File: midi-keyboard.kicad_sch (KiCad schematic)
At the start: 69 parts, among them J1 Conn_01x04, SW1 SW_Push_45deg, SW10 SW_Push_45deg, SW11 SW_Push_45deg, SW12 SW_Push_45deg, SW13 SW_Push_45deg, SW15 SW_Push_45deg, SW16 SW_Push_45deg, SW17 SW_Push_45deg, SW18 SW_Push_45deg, SW19 SW_Push_45deg, SW2 SW_Push_45deg, SW20 SW_Push_45deg, SW22 SW_Push_45deg, SW23 SW_Push_45deg, SW24 SW_Push_45deg, SW25 SW_Push_45deg, SW26 SW_Push_45deg, SW29 SW_Push_45deg, SW3 SW_Push_45deg, SW30 SW_Push_45deg, SW31 SW_Push_45deg, SW32 SW_Push_45deg, SW33 SW_Push_45deg, SW35 SW_Push_45deg, SW36 SW_Push_45deg, SW37 SW_Push_45deg, SW38 SW_Push_45deg, SW39 SW_Push_45deg, SW4 SW_Push_45deg, SW44 SW_Push_45deg, SW5 SW_Push_45deg, SW6 SW_Push_45deg, SW8 SW_Push_45deg, SW9 SW_Push_45deg

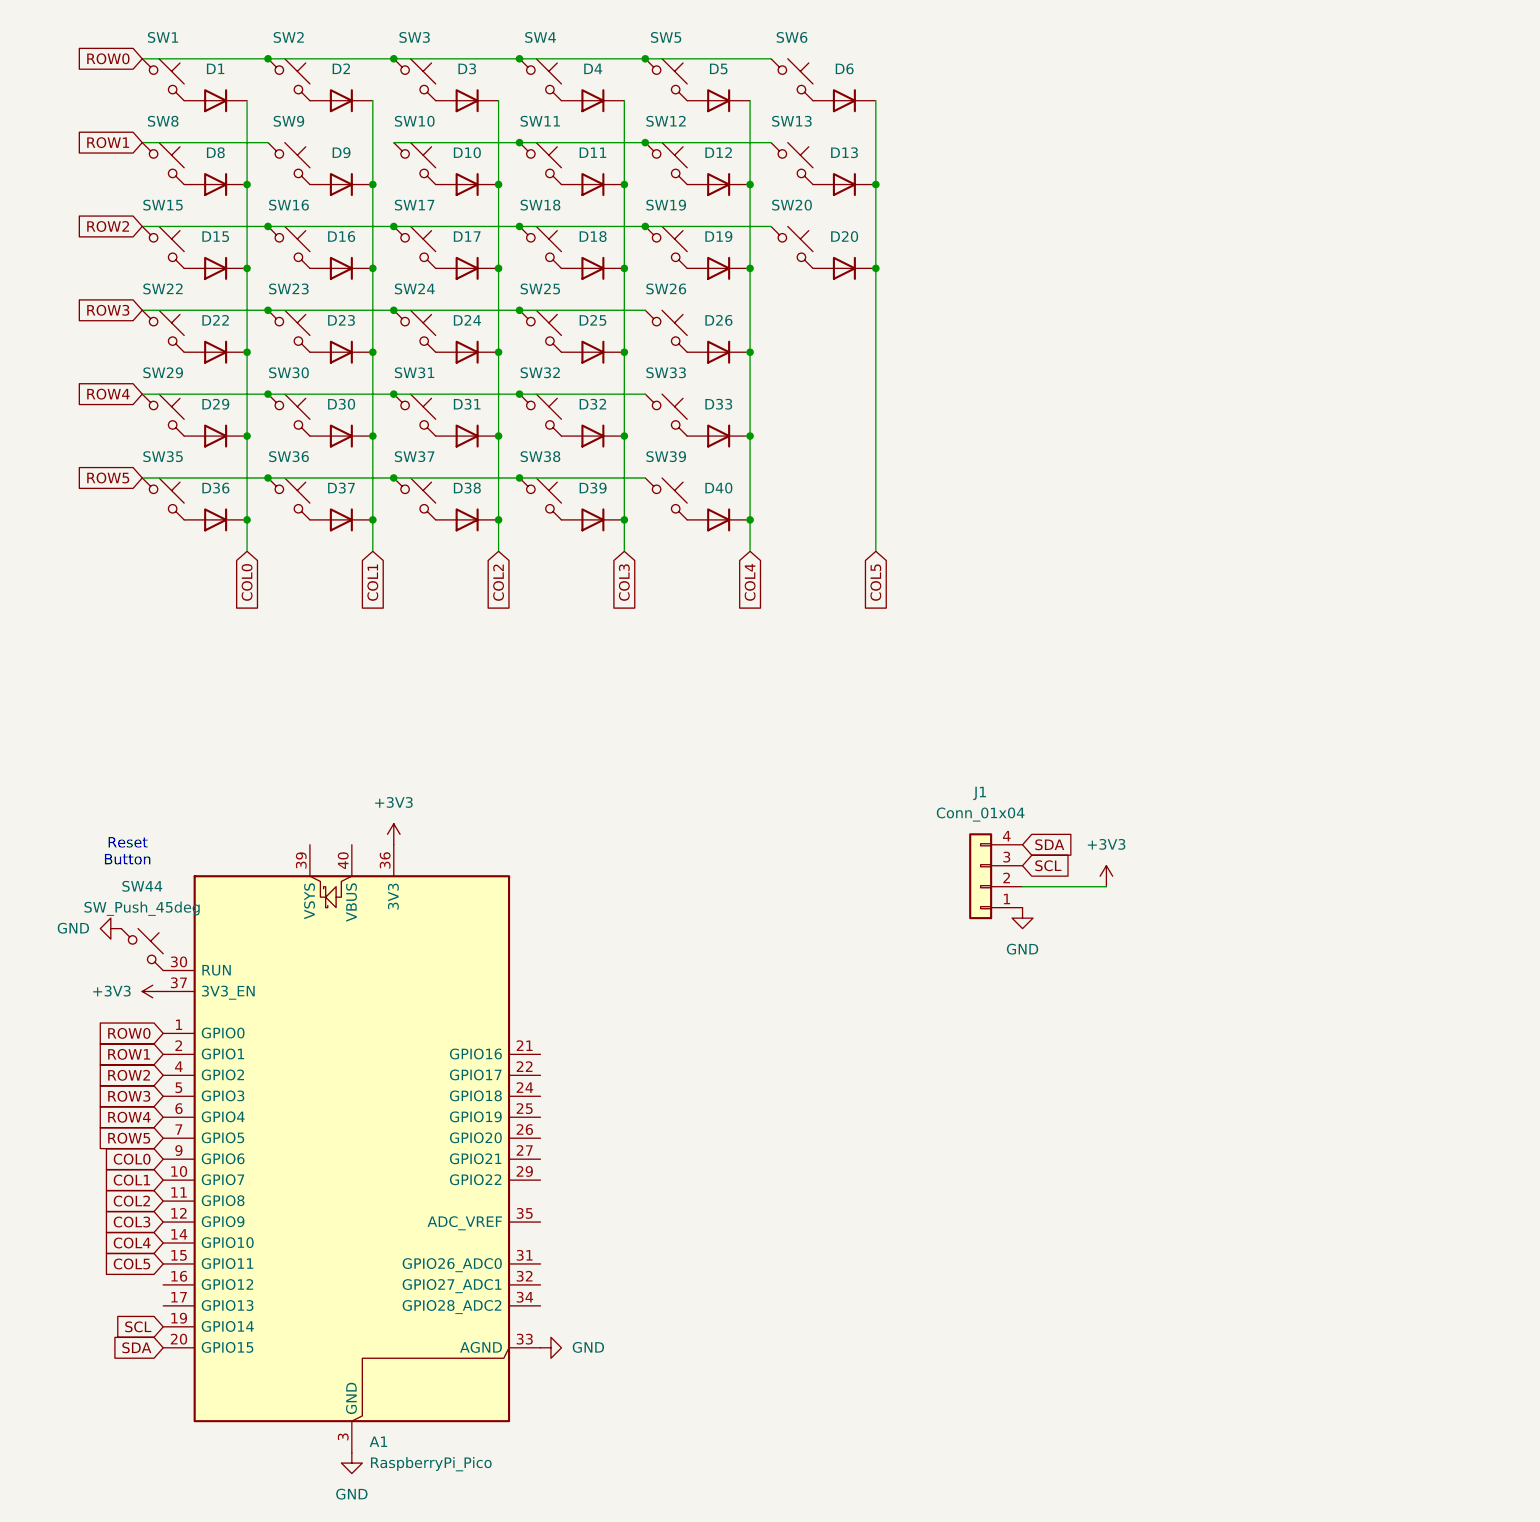
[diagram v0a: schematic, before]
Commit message: finished pcb tracing
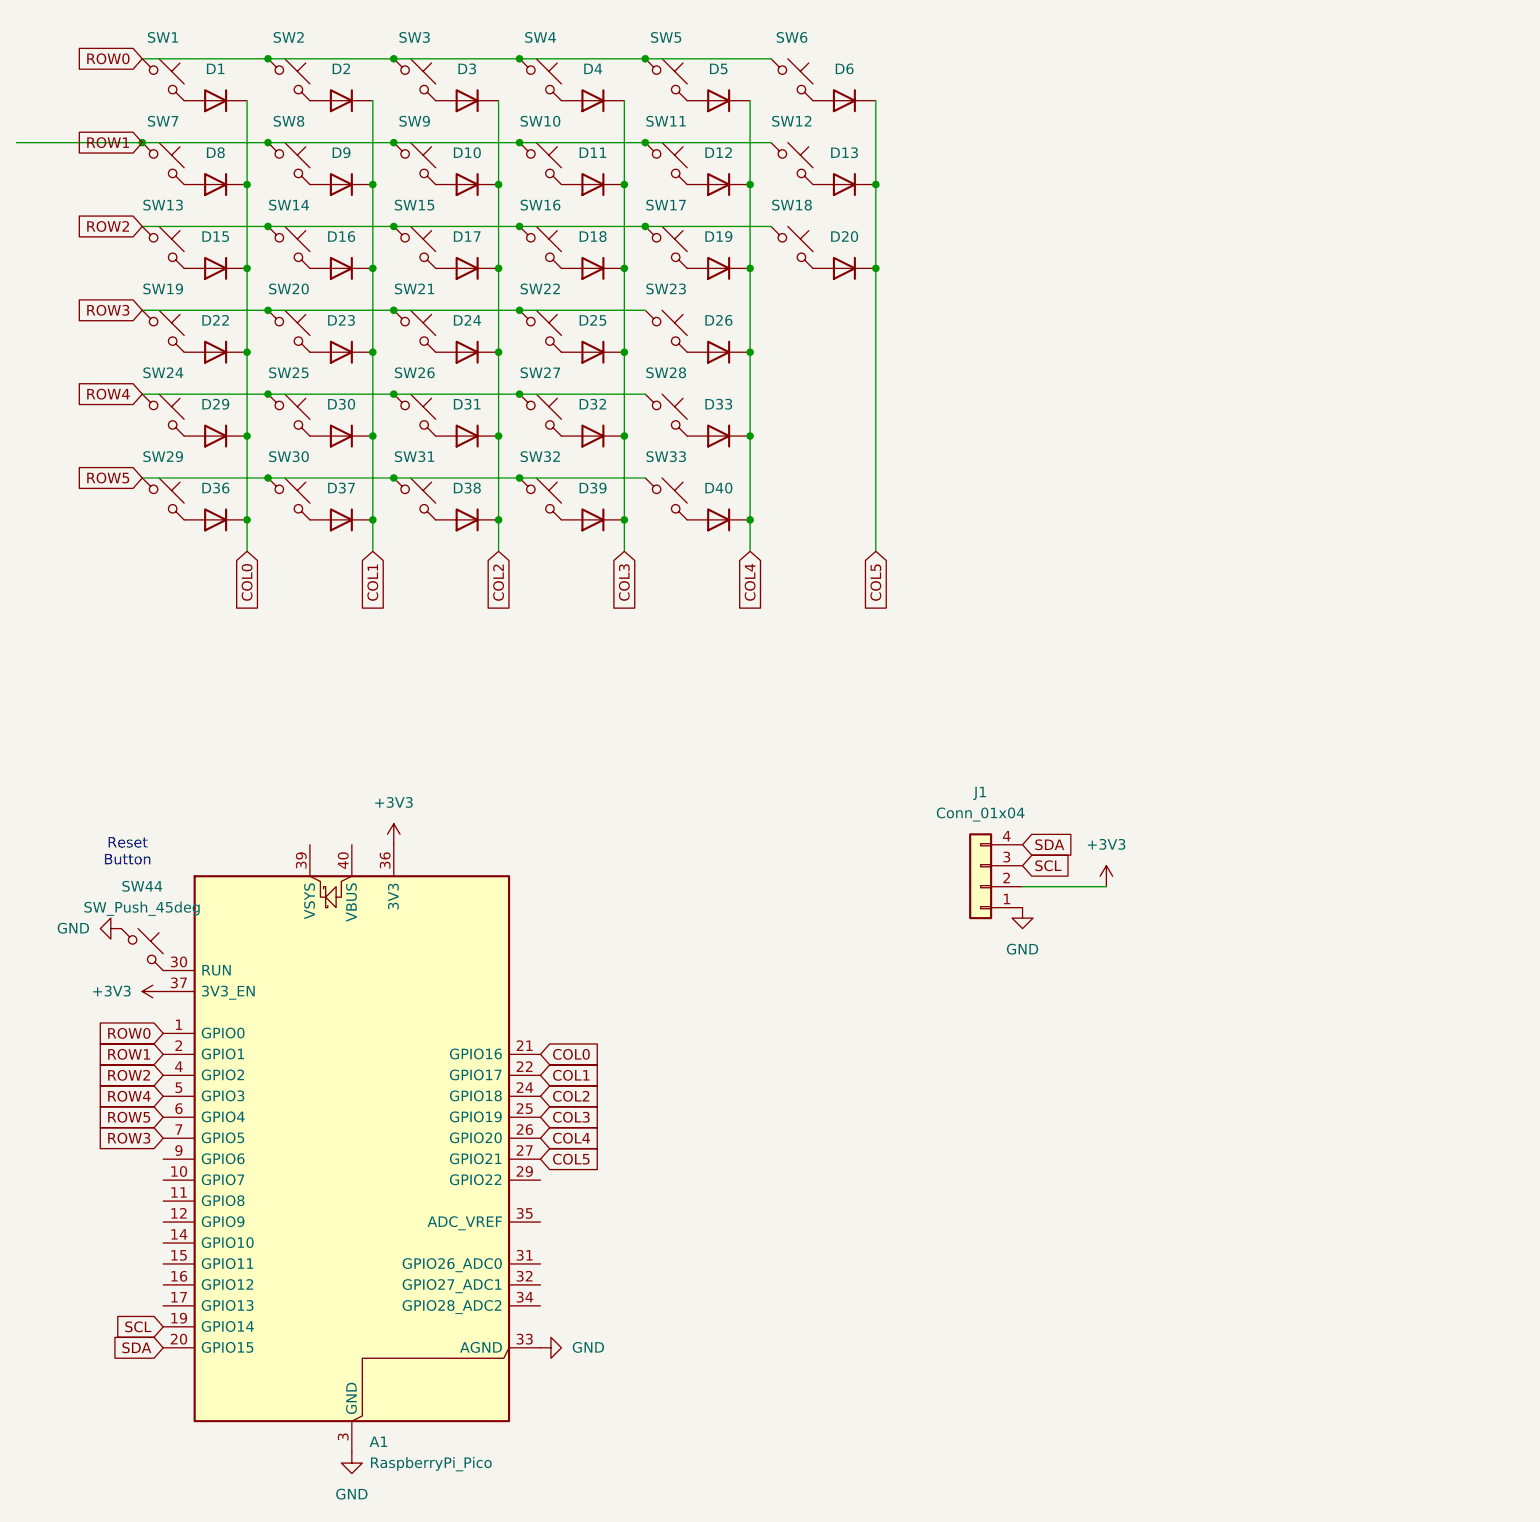
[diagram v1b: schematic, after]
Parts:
- J1: footprint Connector_PinSocket_2.54mm:PinSocket_1x05_P2.54mm_Vertical -> Connector_PinSocket_2.54mm:PinSocket_1x04_P2.54mm_Vertical
- SW44: footprint Button_Switch_Keyboard:SW_Cherry_MX_1.00u_PCB -> Button_Switch_THT:SW_PUSH_6mm
- renumbered SW11 to SW10, SW12 to SW11, SW13 to SW12, SW15 to SW13, SW16 to SW14, SW17 to SW15, SW18 to SW16, SW19 to SW17, SW20 to SW18, SW22 to SW19, SW23 to SW20, SW24 to SW21, SW25 to SW22, SW26 to SW23, SW29 to SW24, SW30 to SW25, SW31 to SW26, SW32 to SW27, SW33 to SW28, SW35 to SW29, SW36 to SW30, SW37 to SW31, SW38 to SW32, SW39 to SW33, SW8 to SW7, SW9 to SW8, SW10 to SW9
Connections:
- net COL0: now also A1.21 (GPIO16); no longer A1.9 (GPIO6)
- net COL1: now also A1.22 (GPIO17); no longer A1.10 (GPIO7)
- net COL2: now also A1.24 (GPIO18); no longer A1.11 (GPIO8)
- net COL3: now also A1.25 (GPIO19); no longer A1.12 (GPIO9)
- net COL4: now also A1.26 (GPIO20); no longer A1.14 (GPIO10)
- net COL5: now also A1.27 (GPIO21); no longer A1.15 (GPIO11)
- net ROW1: now also SW10.1, SW11.1, SW12.1, SW9.1
- net ROW3: now also A1.7 (GPIO5); no longer A1.5 (GPIO3)
- net ROW4: now also A1.5 (GPIO3); no longer A1.6 (GPIO4)
- net ROW5: now also A1.6 (GPIO4); no longer A1.7 (GPIO5)

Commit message: README
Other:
- title: (none) -> MusePad
- moved on the sheet: A1, J1, SW44
